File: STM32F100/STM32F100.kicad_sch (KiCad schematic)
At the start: 7 parts, among them J1 USB_OTG, J2 Screw_Terminal_01x02, U1 STM32F100C4Tx, U2 AZ1117-3.3, Y1 8MHz

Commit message: Add AMS1117 3.3V
add 3.3V voltage regulator
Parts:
- C1: footprint (none) -> Capacitor_SMD:C_0805_2012Metric_Pad1.18x1.45mm_HandSolder
- J1: footprint (none) -> Connector_USB:USB_Micro-AB_Molex_47590-0001
- J2: footprint (none) -> TerminalBlock:TerminalBlock_Altech_AK300-2_P5.00mm
- U2: footprint (none) -> Package_TO_SOT_SMD:SOT-89-3_Handsoldering
- Y1: footprint (none) -> Crystal:Crystal_HC52-U_Vertical
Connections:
- net GND: now also U1.23 (VSS), U1.35 (VSS), U1.47 (VSS), U1.8 (VSSA)
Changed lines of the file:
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@@
     (comment 1 "Author : Dwi Kurniawan")
   )
+  (junction (at 124.46 111.76) (diameter 0) (color 0 0 0 0)
+  )
+  (junction (at 119.38 111.76) (diameter 0) (color 0 0 0 0)
+  )
   (junction (at 66.04 54.61) (diameter 0) (color 0 0 0 0)
   )
+  (junction (at 121.92 111.76) (diameter 0) (color 0 0 0 0)
+  )
   (junction (at 66.04 46.99) (diameter 0) (color 0 0 0 0)
   )
@@
     (stroke (width 0) (type default) (color 0 0 0 0))
   )
+  (wire (pts (xy 121.92 111.76) (xy 119.38 111.76))
+    (stroke (width 0) (type default) (color 0 0 0 0))
+  )
   (wire (pts (xy 30.48 44.45) (xy 30.48 45.72))
     (stroke (width 0) (type default) (color 0 0 0 0))
   )
+  (wire (pts (xy 127 107.95) (xy 127 111.76))
+    (stroke (width 0) (type default) (color 0 0 0 0))
+  )
+  (wire (pts (xy 119.38 111.76) (xy 119.38 114.3))
+    (stroke (width 0) (type default) (color 0 0 0 0))
+  )
+  (wire (pts (xy 119.38 107.95) (xy 119.38 111.76))
+    (stroke (width 0) (type default) (color 0 0 0 0))
+  )
+  (wire (pts (xy 124.46 111.76) (xy 121.92 111.76))
+    (stroke (width 0) (type default) (color 0 0 0 0))
+  )
   (wire (pts (xy 74.93 156.21) (xy 73.66 156.21))
     (stroke (width 0) (type default) (color 0 0 0 0))
@@
     (stroke (width 0) (type default) (color 0 0 0 0))
   )
+  (wire (pts (xy 124.46 107.95) (xy 124.46 111.76))
+    (stroke (width 0) (type default) (color 0 0 0 0))
+  )
+  (wire (pts (xy 127 111.76) (xy 124.46 111.76))
+    (stroke (width 0) (type default) (color 0 0 0 0))
+  )
   (wire (pts (xy 66.04 54.61) (xy 66.04 55.88))
     (stroke (width 0) (type default) (color 0 0 0 0))
@@
     (stroke (width 0) (type default) (color 0 0 0 0))
   )
+  (wire (pts (xy 121.92 107.95) (xy 121.92 111.76))
+    (stroke (width 0) (type default) (color 0 0 0 0))
+  )
   (wire (pts (xy 74.93 161.29) (xy 74.93 156.21))
     (stroke (width 0) (type default) (color 0 0 0 0))
@@
   (wire (pts (xy 66.04 46.99) (xy 106.68 46.99))
     (stroke (width 0) (type default) (color 0 0 0 0))
+  )
+  (symbol (lib_id "power:GND") (at 119.38 114.3 0) (unit 1)
+    (in_bom yes) (on_board yes) (fields_autoplaced)
+    (property "Reference" "#PWR?" (id 0) (at 119.38 120.65 0)
+      (effects (font (size 1.27 1.27)) hide)
+    )
+    (property "Value" "GND" (id 1) (at 119.38 119.38 0))
+    (property "Footprint" "" (id 2) (at 119.38 114.3 0)
+      (effects (font (size 1.27 1.27)) hide)
+    )
+    (property "Datasheet" "" (id 3) (at 119.38 114.3 0)
+      (effects (font (size 1.27 1.27)) hide)
+    )
+    (pin "1")
   )
   (symbol (lib_id "power:GND") (at 74.93 161.29 0) (unit 1)
@@
       (effects (font (size 1.27 1.27)) (justify left))
     )
-    (property "Footprint" "" (id 2) (at 67.0052 63.5 0)
+    (property "Footprint" "Capacitor_SMD:C_0805_2012Metric_Pad1.18x1.45mm_HandSolder" (id 2) (at 67.0052 63.5 0)
       (effects (font (size 1.27 1.27)) hide)
     )
@@
     (property "Reference" "J2" (id 0) (at 68.58 147.32 0))
     (property "Value" "Screw_Terminal_01x02" (id 1) (at 68.58 149.86 0))
-    (property "Footprint" "" (id 2) (at 68.58 156.21 0)
+    (property "Footprint" "TerminalBlock:TerminalBlock_Altech_AK300-2_P5.00mm" (id 2) (at 68.58 156.21 0)
       (effects (font (size 1.27 1.27)) hide)
     )
@@
     (property "Reference" "U2" (id 0) (at 101.6 146.05 0))
     (property "Value" "AZ1117-3.3" (id 1) (at 101.6 148.59 0))
-    (property "Footprint" "" (id 2) (at 101.6 147.32 0)
+    (property "Footprint" "Package_TO_SOT_SMD:SOT-89-3_Handsoldering" (id 2) (at 101.6 147.32 0)
       (effects (font (size 1.27 1.27) italic) hide)
     )
@@
       (effects (font (size 1.27 1.27)) (justify right))
     )
-    (property "Footprint" "" (id 2) (at 66.04 50.8 0)
+    (property "Footprint" "Crystal:Crystal_HC52-U_Vertical" (id 2) (at 66.04 50.8 0)
       (effects (font (size 1.27 1.27)) hide)
     )
@@
     (property "Reference" "J1" (id 0) (at 33.02 21.59 0))
     (property "Value" "USB_OTG" (id 1) (at 33.02 24.13 0))
-    (property "Footprint" "" (id 2) (at 36.83 35.56 0)
+    (property "Footprint" "Connector_USB:USB_Micro-AB_Molex_47590-0001" (id 2) (at 36.83 35.56 0)
       (effects (font (size 1.27 1.27)) hide)
     )
@@
       (reference "#PWR0106") (unit 1) (value "GND") (footprint "")
     )
+    (path "/168c3afe-5e84-4665-a901-7ae461efa5be"
+      (reference "#PWR?") (unit 1) (value "GND") (footprint "")
+    )
     (path "/471652a3-3684-463f-ae23-da297a165c12"

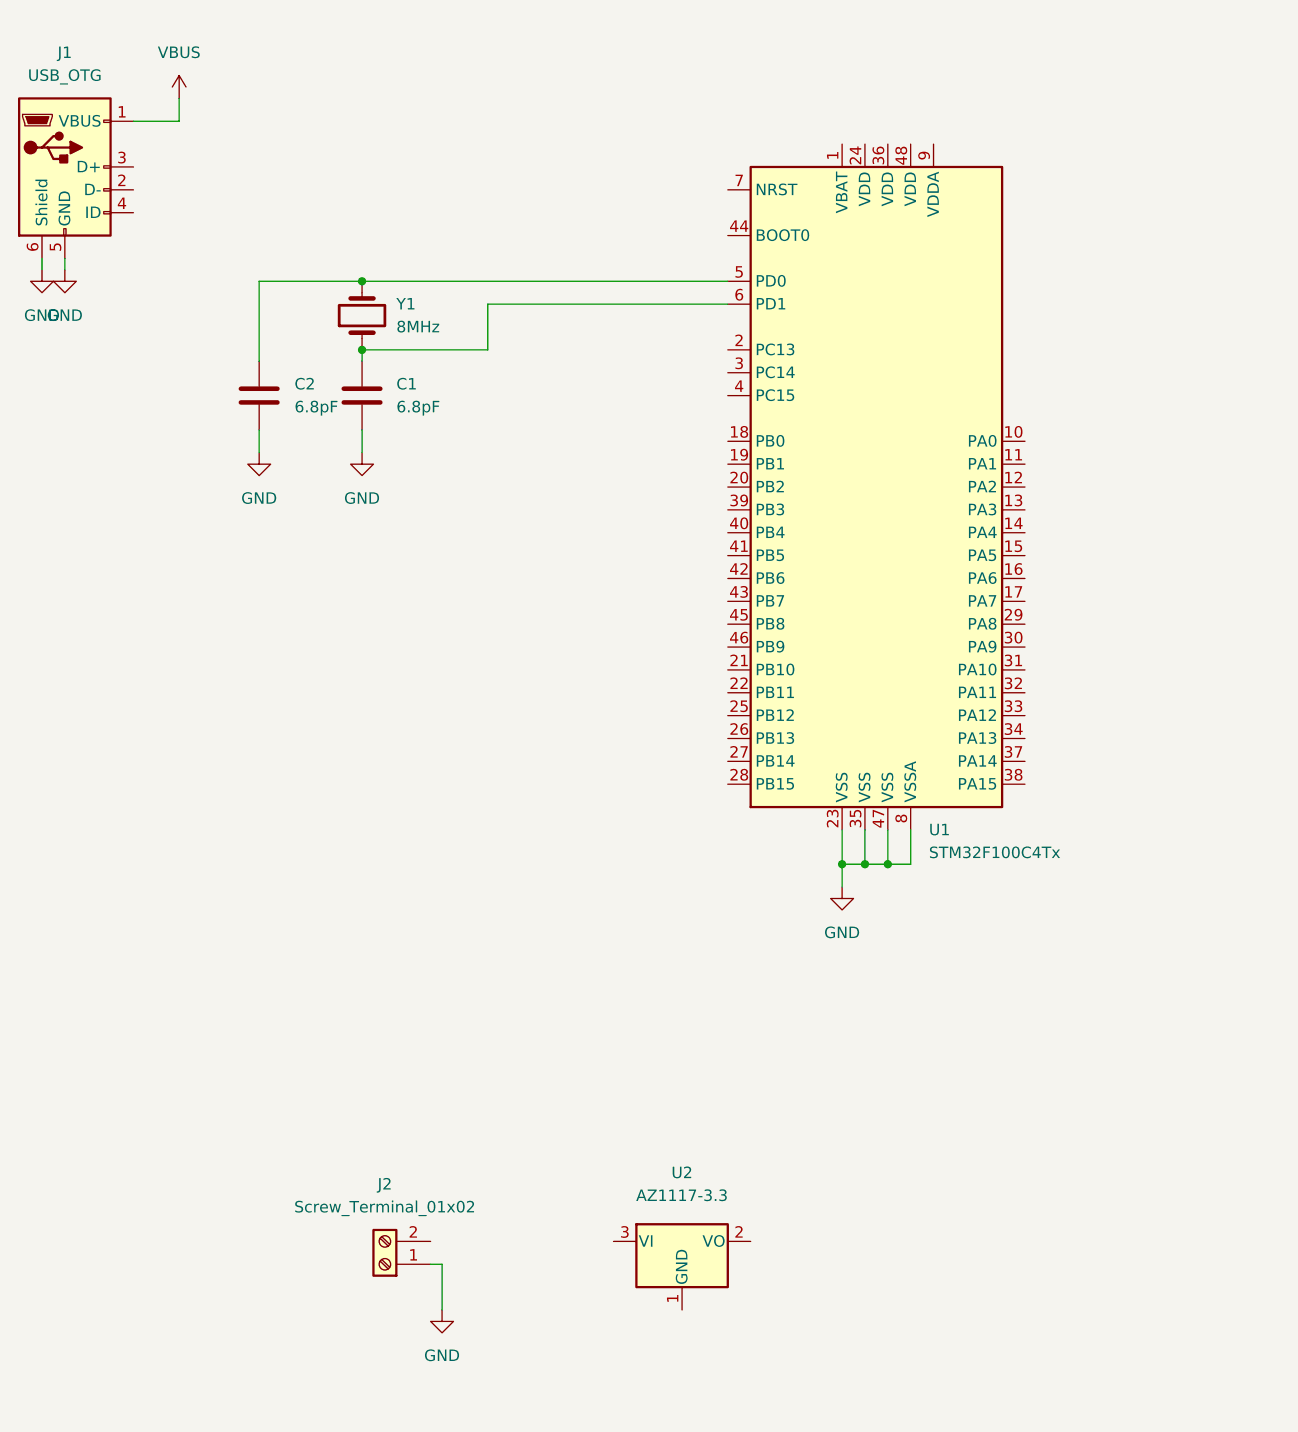
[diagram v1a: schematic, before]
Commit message: Add IO pin header
Add IO Pinheader
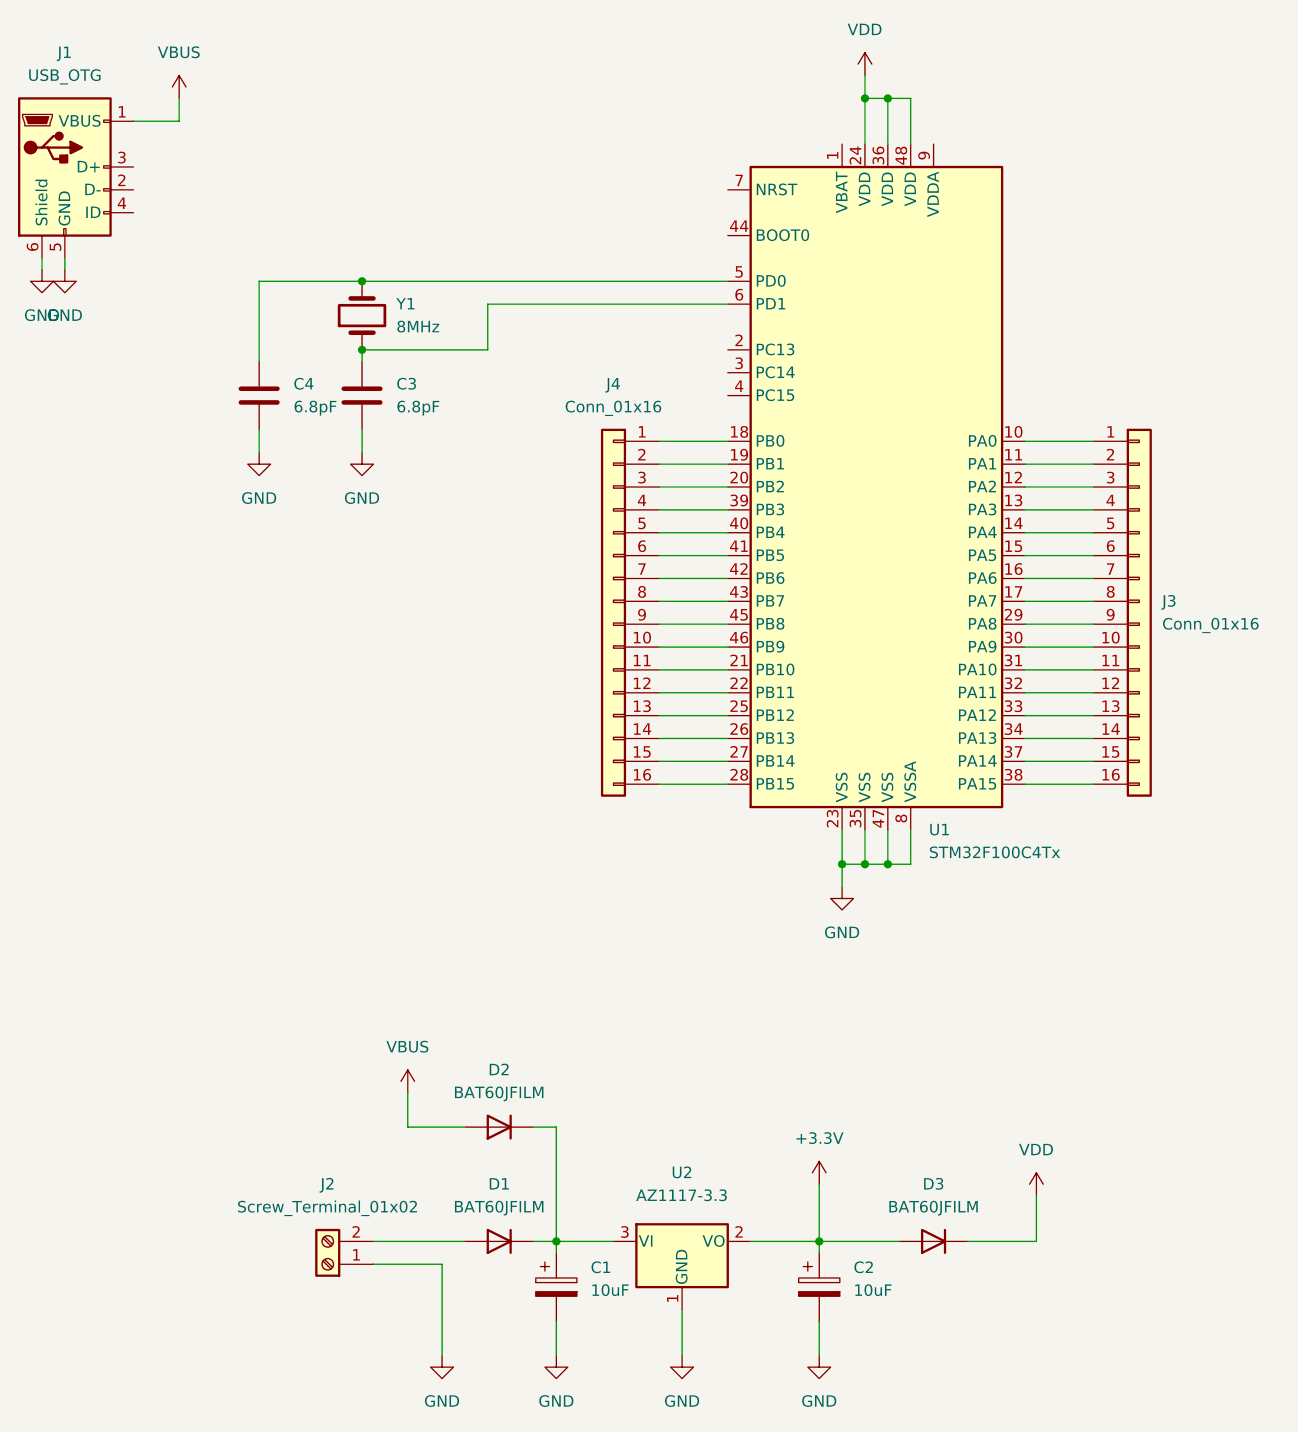
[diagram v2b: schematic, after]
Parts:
- added C1, C2: 10uF, symbol Device:C_Polarized
- added D1: BAT60JFILM, symbol Device:D
- added D2, D3: BAT60JFILM, Diode_SMD:D_2010_5025Metric, symbol Device:D
- added J3: Conn_01x16, symbol Connector_Generic:Conn_01x16
- added J4: Conn_01x16, Connector_Molex:Molex_KK-254_AE-6410-16A_1x16_P2.54mm_Vertical, symbol Connector_Generic:Conn_01x16
- renumbered C1 to C3, C2 to C4
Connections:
- net GND: now also U2.1 (GND), C1.2, C2.2
- net VBUS: now also D2.2 (A)
- net at U1.10 (PA0): now also J3.1 (Pin_1)
- net at U1.11 (PA1): now also J3.2 (Pin_2)
- net at U1.12 (PA2): now also J3.3 (Pin_3)
- net at U1.13 (PA3): now also J3.4 (Pin_4)
- net at U1.14 (PA4): now also J3.5 (Pin_5)
- net at U1.15 (PA5): now also J3.6 (Pin_6)
- net at U1.16 (PA6): now also J3.7 (Pin_7)
- net at U1.17 (PA7): now also J3.8 (Pin_8)
- net at U1.18 (PB0): now also J4.1 (Pin_1)
- net at U1.19 (PB1): now also J4.2 (Pin_2)
- net at U1.20 (PB2): now also J4.3 (Pin_3)
- net at U1.21 (PB10): now also J4.11 (Pin_11)
- net at U1.22 (PB11): now also J4.12 (Pin_12)
- net VDD: now reaches U1.24 (VDD)
- net VDD: now also U1.36 (VDD), U1.48 (VDD), D3.1 (K)
- net at U1.25 (PB12): now also J4.13 (Pin_13)
- net at U1.26 (PB13): now also J4.14 (Pin_14)
- net at U1.27 (PB14): now also J4.15 (Pin_15)
- net at U1.28 (PB15): now also J4.16 (Pin_16)
- net at U1.29 (PA8): now also J3.9 (Pin_9)
- net at U1.30 (PA9): now also J3.10 (Pin_10)
- net at U1.31 (PA10): now also J3.11 (Pin_11)
- net at U1.32 (PA11): now also J3.12 (Pin_12)
- net at U1.33 (PA12): now also J3.13 (Pin_13)
- net at U1.34 (PA13): now also J3.14 (Pin_14)
- net at U1.37 (PA14): now also J3.15 (Pin_15)
- net at U1.38 (PA15): now also J3.16 (Pin_16)
- net at U1.39 (PB3): now also J4.4 (Pin_4)
- net at U1.40 (PB4): now also J4.5 (Pin_5)
- net at U1.41 (PB5): now also J4.6 (Pin_6)
- net at U1.42 (PB6): now also J4.7 (Pin_7)
- net at U1.43 (PB7): now also J4.8 (Pin_8)
- net at U1.45 (PB8): now also J4.9 (Pin_9)
- net at U1.46 (PB9): now also J4.10 (Pin_10)
- net at J2.2 (Pin_2): now also D1.2 (A)
- net +3.3V: now reaches U2.2 (VO)
- net +3.3V: now also C2.1, D3.2 (A)
- net at U2.3 (VI): now also C1.1, D1.1 (K), D2.1 (K)
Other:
- moved on the sheet: J2
